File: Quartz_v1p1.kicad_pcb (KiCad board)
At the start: 6 copper layers, 254 x 130 mm, 1245 parts, among them J1 5747847-6, J2 5747847-6, J3 Conn_02x10_Odd_Even, J4 Conn_02x10_Odd_Even, J5 PPS IN, J6 WP Jumper, K1001 EE2-12TNU-L, K101 EE2-12TNU-L, K1101 EE2-12TNU-L, K1201 EE2-12TNU-L, K1301 EE2-12TNU-L, K1401 EE2-12TNU-L, K1501 EE2-12TNU-L, K1601 EE2-12TNU-L, K1701 EE2-12TNU-L, K1801 EE2-12TNU-L, K1901 EE2-12TNU-L, K2001 EE2-12TNU-L, K201 EE2-12TNU-L, K2101 EE2-12TNU-L, K2201 EE2-12TNU-L, K2301 EE2-12TNU-L, K2401 EE2-12TNU-L, K2501 EE2-12TNU-L, K2601 EE2-12TNU-L, K2701 EE2-12TNU-L, K2801 EE2-12TNU-L, K2901 EE2-12TNU-L, K3001 EE2-12TNU-L, K301 EE2-12TNU-L, K3101 EE2-12TNU-L, K3201 EE2-12TNU-L, K401 EE2-12TNU-L, K501 EE2-12TNU-L, K601 EE2-12TNU-L, K701 EE2-12TNU-L, K801 EE2-12TNU-L, K901 EE2-12TNU-L, P1 ASP-134604-01, P2 ASP-134604-01, Q1 FDN335N, Q2 FDN335N, Q3 FDMC510P, U1 AD7768, U10 AD7768, U1001 INA851, U101 INA851, U11 ADR4540, U1101 INA851, U12 ADA4841-1, U1201 INA851, U13 AMC7823IRTAR, U1301 INA851, U14 MAX4896, U1401 INA851, U15 MAX4896, U1501 INA851, U16 SI5330B-B00206-GM, U1601 INA851, U17 MAX4896, U1701 INA851, U18 MAX4896, U1801 INA851, U19 MAX4896, U1901 INA851, U2 ADR4540, U20 MAX4896, U2001 INA851, U201 INA851, U21 MAX4896, U2101 INA851, U22 74AVC4T245, U2201 INA851, U23 MAX4896, U2301 INA851, U24 74AVC4T245, U2401 INA851, U25 74LVC8T245, U2501 INA851, U26 74AVC4T245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

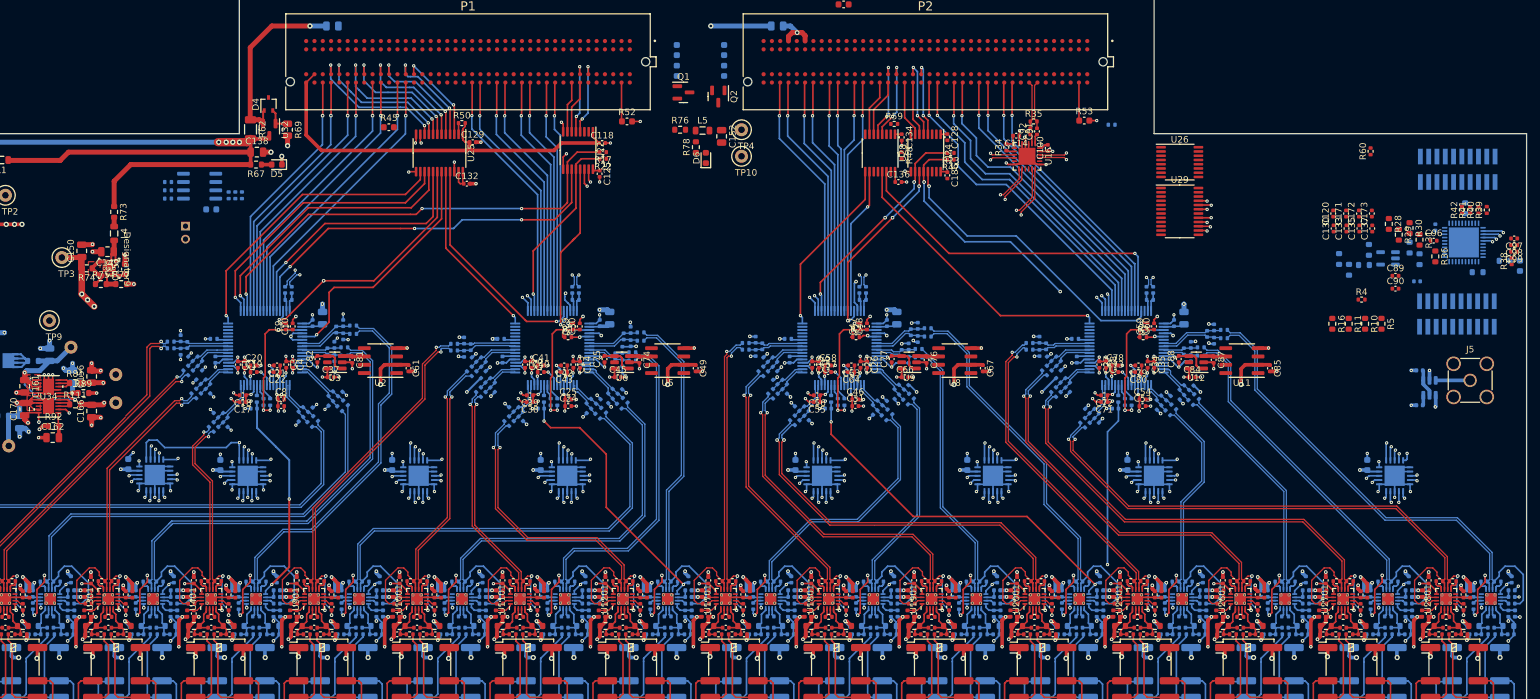
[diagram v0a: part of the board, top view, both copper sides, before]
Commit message: Push Version before ADC change from 1.8V to 2.5V I/O
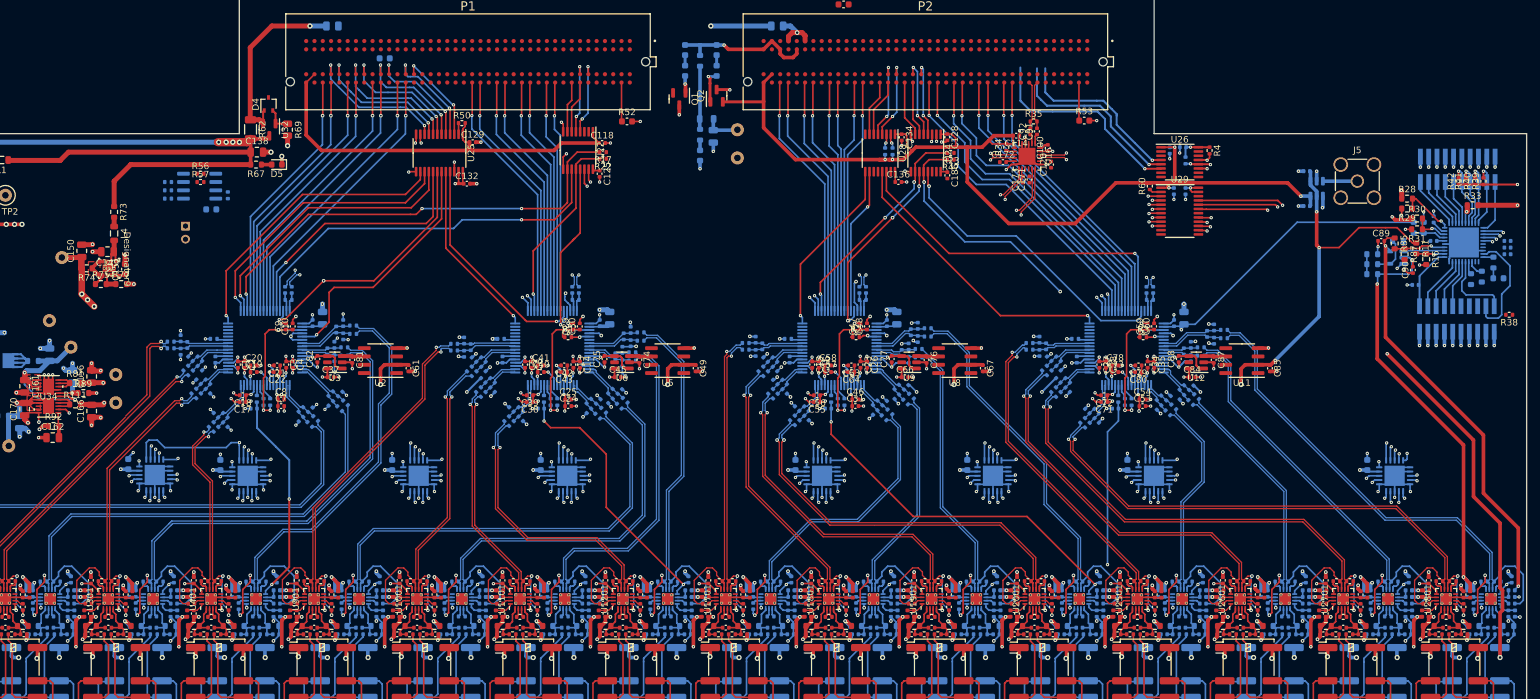
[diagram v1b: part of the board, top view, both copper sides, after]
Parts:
- C130, C133, C135, C137, C152, C96, C97, C98, C99, D6, L5, R10, R36, R45, R48, R5, R59, R76, R78, TP10, TP3, TP4, TP9: moved to B.Cu
- R33, R56, R57, R85, R87: moved to F.Cu
- moved C172 55.1 mm to (257.7, 116.8), turned to 0 degrees
- moved C173 53.7 mm to (260.7, 119.5)
- moved C171 48.7 mm to (261.7, 119.5)
- moved C120 43.8 mm to (265.0, 117.2)
- moved C124 35.0 mm to (304.2, 118.2)
- moved J5 35.0 mm to (311.9, 119.8)
- moved C123 35.0 mm to (304.2, 123.6)
- moved U37 35.0 mm to (305.7, 120.9)
- moved R60 34.2 mm to (280.2, 120.5)
- moved R4 32.6 mm to (289.3, 115.1), turned to -90 degrees
- moved C137 29.1 mm to (285.6, 121.3)
- moved C135 29.0 mm to (283.8, 121.3)
- moved C133 27.9 mm to (285.2, 114.6), turned to 0 degrees
- moved C130 27.8 mm to (283.2, 115.1)
- moved R16 17.4 mm to (322.5, 131.7)
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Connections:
- net /Channel01/FMC_INA_Out+ renamed /Channel01/Housekeeping_INA_Out+
- net /Channel01/FMC_INA_Out- renamed /Channel01/Housekeeping_INA_Out-
- net /Channel02/FMC_INA_Out+ renamed /Channel02/Housekeeping_INA_Out+
- net /Channel02/FMC_INA_Out- renamed /Channel02/Housekeeping_INA_Out-
- net /Channel03/FMC_INA_Out+ renamed /Channel03/Housekeeping_INA_Out+
- net /Channel03/FMC_INA_Out- renamed /Channel03/Housekeeping_INA_Out-
- net /Channel04/FMC_INA_Out+ renamed /Channel04/Housekeeping_INA_Out+
- net /Channel04/FMC_INA_Out- renamed /Channel04/Housekeeping_INA_Out-
- net /Channel05/FMC_INA_Out+ renamed /Channel05/Housekeeping_INA_Out+
- net /Channel05/FMC_INA_Out- renamed /Channel05/Housekeeping_INA_Out-
- net /Channel06/FMC_INA_Out+ renamed /Channel06/Housekeeping_INA_Out+
- net /Channel06/FMC_INA_Out- renamed /Channel06/Housekeeping_INA_Out-
- net /Channel07/FMC_INA_Out+ renamed /Channel07/Housekeeping_INA_Out+
- net /Channel07/FMC_INA_Out- renamed /Channel07/Housekeeping_INA_Out-
- net /Channel08/FMC_INA_Out+ renamed /Channel08/Housekeeping_INA_Out+
- net /Channel08/FMC_INA_Out- renamed /Channel08/Housekeeping_INA_Out-
- net /Channel09/FMC_INA_Out+ renamed /Channel09/Housekeeping_INA_Out+
- net /Channel09/FMC_INA_Out- renamed /Channel09/Housekeeping_INA_Out-
- net /Channel10/FMC_INA_Out+ renamed /Channel10/Housekeeping_INA_Out+
- net /Channel10/FMC_INA_Out- renamed /Channel10/Housekeeping_INA_Out-
- net /Channel11/FMC_INA_Out+ renamed /Channel11/Housekeeping_INA_Out+
- net /Channel11/FMC_INA_Out- renamed /Channel11/Housekeeping_INA_Out-
- net /Channel12/FMC_INA_Out+ renamed /Channel12/Housekeeping_INA_Out+
- net /Channel12/FMC_INA_Out- renamed /Channel12/Housekeeping_INA_Out-
- net /Channel13/FMC_INA_Out+ renamed /Channel13/Housekeeping_INA_Out+
- net /Channel13/FMC_INA_Out- renamed /Channel13/Housekeeping_INA_Out-
- net /Channel14/FMC_INA_Out+ renamed /Channel14/Housekeeping_INA_Out+
- net /Channel14/FMC_INA_Out- renamed /Channel14/Housekeeping_INA_Out-
- net /Channel15/FMC_INA_Out+ renamed /Channel15/Housekeeping_INA_Out+
- net /Channel15/FMC_INA_Out- renamed /Channel15/Housekeeping_INA_Out-
- net /Channel16/FMC_INA_Out+ renamed /Channel16/Housekeeping_INA_Out+
- net /Channel16/FMC_INA_Out- renamed /Channel16/Housekeeping_INA_Out-
- net /Channel17/FMC_INA_Out+ renamed /Channel17/Housekeeping_INA_Out+
- net /Channel17/FMC_INA_Out- renamed /Channel17/Housekeeping_INA_Out-
- net /Channel18/FMC_INA_Out+ renamed /Channel18/Housekeeping_INA_Out+
- net /Channel18/FMC_INA_Out- renamed /Channel18/Housekeeping_INA_Out-
- net /Channel19/FMC_INA_Out+ renamed /Channel19/Housekeeping_INA_Out+
- net /Channel19/FMC_INA_Out- renamed /Channel19/Housekeeping_INA_Out-
- net /Channel20/FMC_INA_Out+ renamed /Channel20/Housekeeping_INA_Out+
- net /Channel20/FMC_INA_Out- renamed /Channel20/Housekeeping_INA_Out-
- net /Channel21/FMC_INA_Out+ renamed /Channel21/Housekeeping_INA_Out+
- net /Channel21/FMC_INA_Out- renamed /Channel21/Housekeeping_INA_Out-
- net /Channel22/FMC_INA_Out+ renamed /Channel22/Housekeeping_INA_Out+
- net /Channel22/FMC_INA_Out- renamed /Channel22/Housekeeping_INA_Out-
- net /Channel23/FMC_INA_Out+ renamed /Channel23/Housekeeping_INA_Out+
- net /Channel23/FMC_INA_Out- renamed /Channel23/Housekeeping_INA_Out-
- net /Channel24/FMC_INA_Out+ renamed /Channel24/Housekeeping_INA_Out+
- net /Channel24/FMC_INA_Out- renamed /Channel24/Housekeeping_INA_Out-
- net /Channel25/FMC_INA_Out+ renamed /Channel25/Housekeeping_INA_Out+
- net /Channel25/FMC_INA_Out- renamed /Channel25/Housekeeping_INA_Out-
- net /Channel26/FMC_INA_Out+ renamed /Channel26/Housekeeping_INA_Out+
- net /Channel26/FMC_INA_Out- renamed /Channel26/Housekeeping_INA_Out-
- net /Channel27/FMC_INA_Out+ renamed /Channel27/Housekeeping_INA_Out+
- net /Channel27/FMC_INA_Out- renamed /Channel27/Housekeeping_INA_Out-
- net /Channel28/FMC_INA_Out+ renamed /Channel28/Housekeeping_INA_Out+
- net /Channel28/FMC_INA_Out- renamed /Channel28/Housekeeping_INA_Out-
- net /Channel29/FMC_INA_Out+ renamed /Channel29/Housekeeping_INA_Out+
- net /Channel29/FMC_INA_Out- renamed /Channel29/Housekeeping_INA_Out-
- net /Channel30/FMC_INA_Out+ renamed /Channel30/Housekeeping_INA_Out+
- net /Channel30/FMC_INA_Out- renamed /Channel30/Housekeeping_INA_Out-
- net /Channel31/FMC_INA_Out+ renamed /Channel31/Housekeeping_INA_Out+
- net /Channel31/FMC_INA_Out- renamed /Channel31/Housekeeping_INA_Out-
- net /Channel32/FMC_INA_Out+ renamed /Channel32/Housekeeping_INA_Out+
- net /Channel32/FMC_INA_Out- renamed /Channel32/Housekeeping_INA_Out-
- J3 pad 11: /Housekeeping/DAC3 -> unconnected-(J3-Pin_11-Pad11)
- J3 pad 13: /Housekeeping/DAC2 -> unconnected-(J3-Pin_13-Pad13)
- J3 pad 15: /Housekeeping/DAC1 -> unconnected-(J3-Pin_15-Pad15)
- J3 pad 17: /Housekeeping/DAC0 -> /Housekeeping/GPIO4
- J3 pad 3: /Housekeeping/DAC7 -> /Housekeeping/DAC3
- J3 pad 5: /Housekeeping/DAC6 -> /Housekeeping/DAC2
- J3 pad 7: /Housekeeping/DAC5 -> /Housekeeping/DAC1
- J3 pad 9: /Housekeeping/DAC4 -> /Housekeeping/DAC0
- R30 pad 1: V12P0V_bus -> +12V
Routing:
- net P2_VADJ: track 8.09 -> 155.5 mm, vias 0 -> 5
- net VDD3P3V: track 362.7 -> 475.8 mm, vias 8 -> 13
- net GND: track 904.0 -> 983.2 mm, vias 484 -> 526
- net +12V: track 888.3 -> 967.1 mm, vias 68 -> 70
- net P2_Timing_Input: track 1.81 -> 66.4 mm
- net 15V+: track 439.0 -> 503.1 mm, vias 18 -> 19
- net 15V-: track 390.5 -> 452.0 mm, vias 17 -> 19
- net AMC7823_SPI_MISO: track 2.15 -> 53.9 mm, vias 1 -> 2
- net P2_Relay_ShiftData: track 0.00 -> 50.2 mm, vias 0 -> 1
- net P2_MAX4896_~{Reset}: track 0.00 -> 48.7 mm, vias 0 -> 1
- net AMC7823_SPI_SCLK: track 4.56 -> 52.5 mm
- net +5V: track 767.9 -> 814.2 mm, vias 83 -> 86
- net AMC7823_SPI_MOSI: track 4.81 -> 50.8 mm
- net P2_MAX4896_~{CS}: track 0.00 -> 45.4 mm, vias 0 -> 1
- net VDD1P8V: track 345.6 -> 389.7 mm, vias 15 -> 17
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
